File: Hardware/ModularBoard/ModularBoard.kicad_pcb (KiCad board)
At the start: 2 copper layers, 22.9 x 48.3 mm, 16 parts, among them IC1 WS2811-5050, IC2 WS2811-5050, IC3 WS2811-5050, IC4 WS2811-5050, IC5 ATTINY85-P, J1 GSG-USB-MICRO-B, K1 CONN_3, K2 CONN_3, K3 CONN_3, K4 CONN_3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

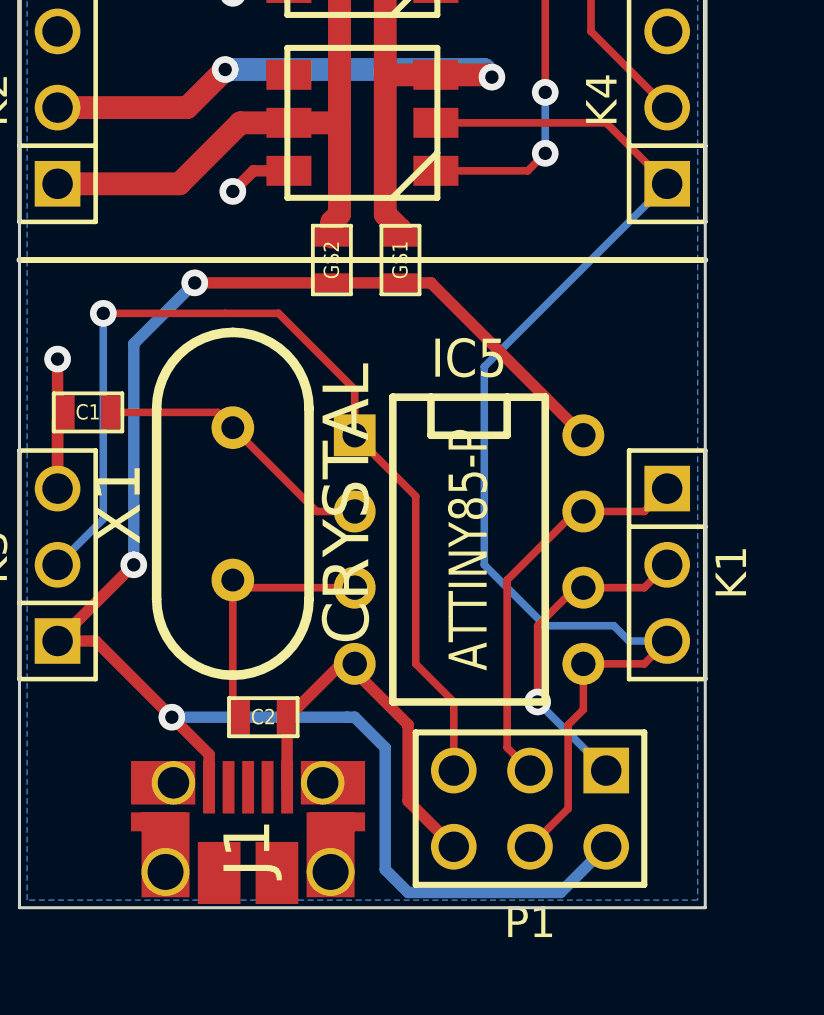
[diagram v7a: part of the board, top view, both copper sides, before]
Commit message: added a bit of space between MCU and ICSP header, ground plane fills better now
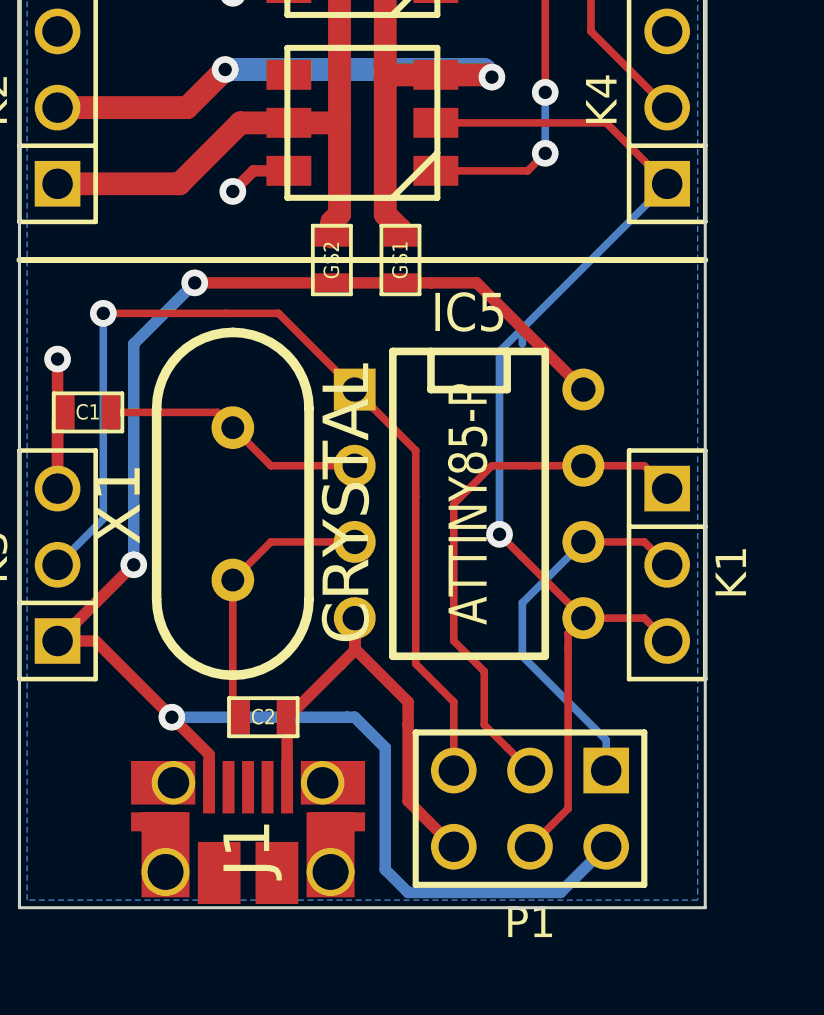
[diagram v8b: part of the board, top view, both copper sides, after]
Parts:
- moved IC5 1.52 mm to (230.9, 154.2)
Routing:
- net /SCK: track 13.3 -> 17.9 mm
- net GND: track 27.7 -> 30.5 mm
- net /MOSI: track 40.9 -> 39.0 mm, vias 0 -> 1
- net /MISO: track 10.9 -> 12.7 mm, vias 1 -> 0
- net +5V: track 56.5 -> 55.9 mm
- net N-0000017: track 9.50 -> 8.86 mm
